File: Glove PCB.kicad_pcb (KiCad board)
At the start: 4 copper layers, 50 x 40 mm, 60 parts, among them IC2 MAX11128ATI+, IC3 MAX11128ATI+, J1 USB_B_Micro, J2 Conn_01x06_Female, J3 Conn_01x04_Female, J4 Conn_01x02_Female, J5 Conn_01x06_Female, J6 Conn_01x04_Female, J7 Conn_02x07_Odd_Even, Q1 DMG2305, Q2 BSS138, Q3 BSS138, SW1 TS-1109S-B-B, U1 MCP73831T-2ACI_OT, U2 REF3030, U3 113990582

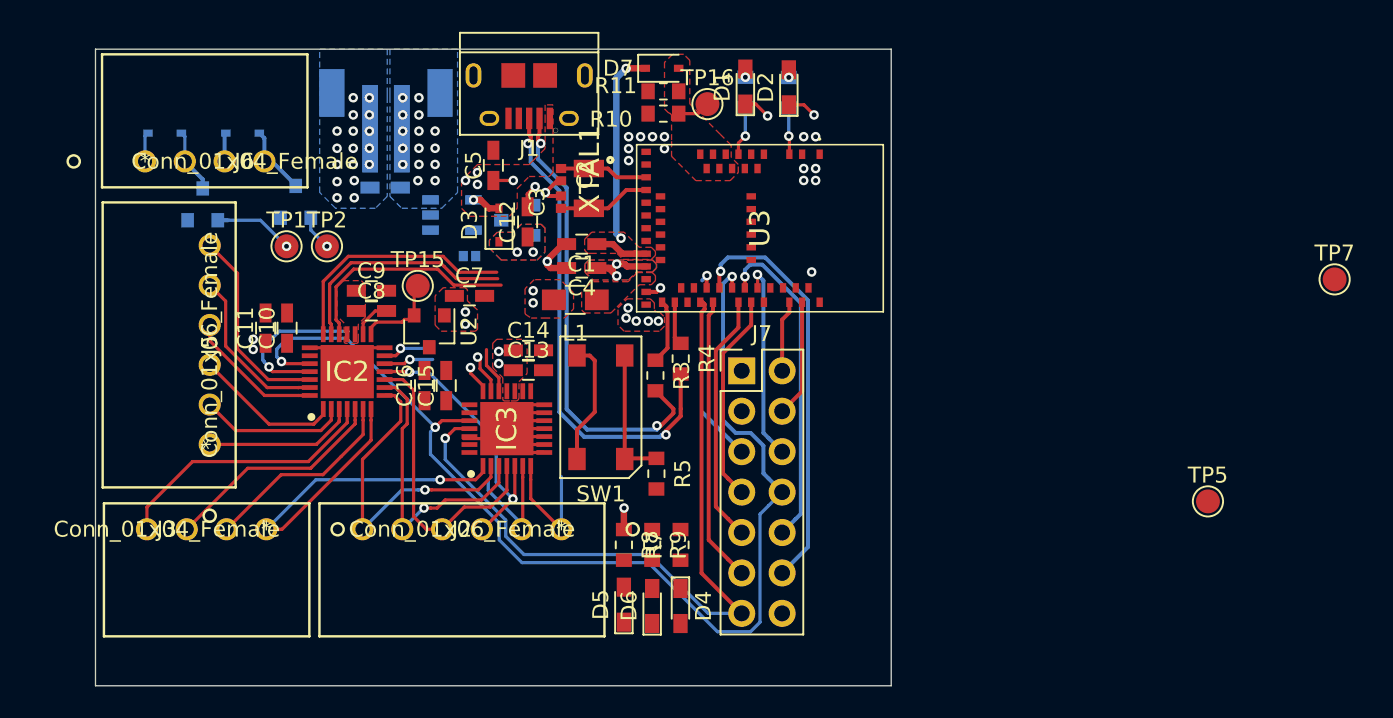
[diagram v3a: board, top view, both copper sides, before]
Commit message: Added high side R for sensors and buck-boost. Replaced 3.0V VRef with LDO. BOM rev 1. Finished layout. TODO: Silkscreen.
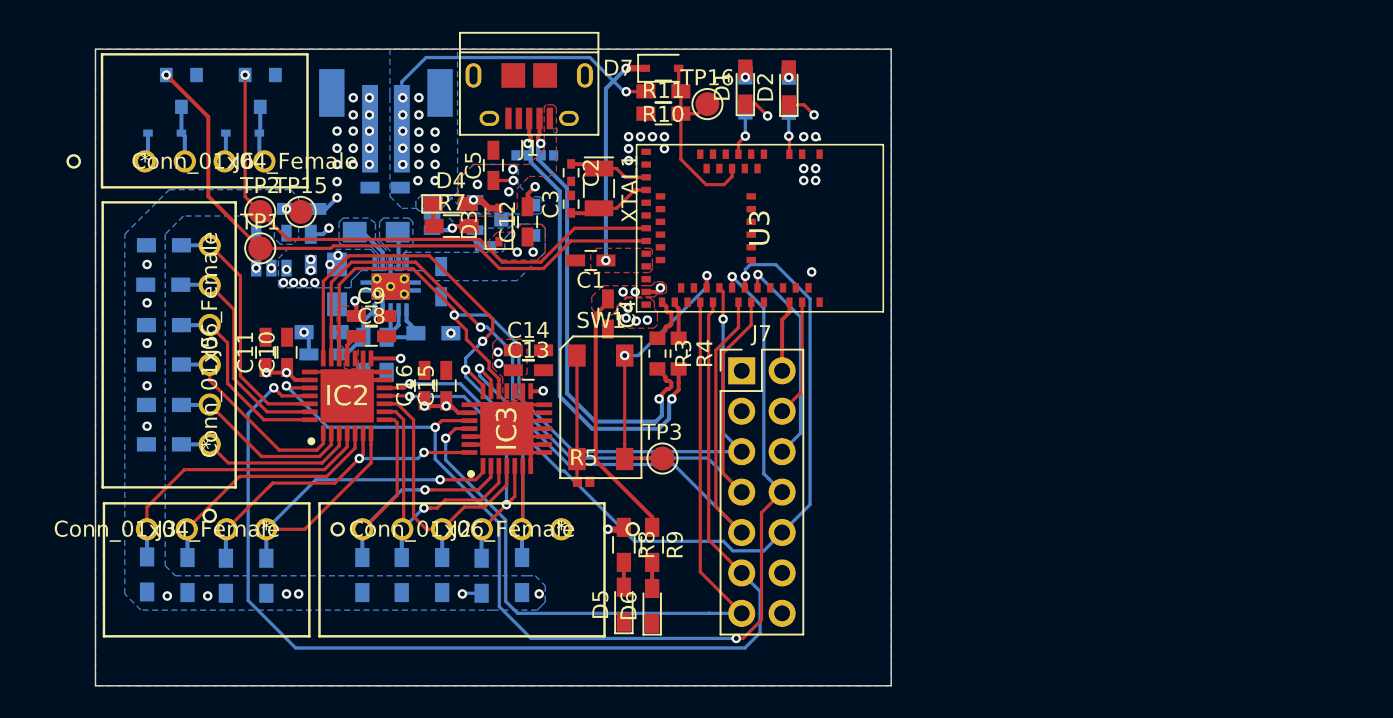
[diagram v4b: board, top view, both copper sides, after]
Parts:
- removed TP5: NFC1, TestPoint:TestPoint_Pad_D1.5mm
- removed TP7: NFC2, TestPoint:TestPoint_Pad_D1.5mm
- added C17: 10uF, Capacitors_SMD:C_0603_HandSoldering, B.Cu at (41.7, 169.6)
- added C18: 1pF, Capacitors_SMD:C_0603_HandSoldering, B.Cu at (34.4, 174.2)
- added C19: 33uF, Capacitors_SMD:C_0805_HandSoldering, B.Cu at (35.2, 169.8)
- added C20: 1uF, Capacitors_SMD:C_0603_HandSoldering, B.Cu at (33.0, 165.0)
- added D10: PGB1010402KR, Diode_SMD:D_0402_1005Metric, B.Cu at (46.8, 161.7)
- added D11: PGB1010402KR, Diode_SMD:D_0402_1005Metric, B.Cu at (48.4, 161.7)
- added R12: 100k, Resistors_SMD:R_0603_HandSoldering, B.Cu at (41.2, 172.8)
- added R13: 130k, Resistors_SMD:R_0603_HandSoldering, B.Cu at (38.3, 174.2)
- added R14: 178k, Resistors_SMD:R_0603_HandSoldering, B.Cu at (36.8, 174.2)
- added R15: 1Meg, Resistors_SMD:R_0603_HandSoldering, B.Cu at (34.2, 172.8)
- added R16: 220, Resistors_SMD:R_0603_HandSoldering, B.Cu at (24.3, 167.3)
- added R17: 220, Resistors_SMD:R_0603_HandSoldering, B.Cu at (24.3, 169.8)
- added R18: 220, Resistors_SMD:R_0603_HandSoldering, B.Cu at (24.3, 172.3)
- added R19: 220, Resistors_SMD:R_0603_HandSoldering, B.Cu at (24.3, 174.8)
- added R20: 220, Resistors_SMD:R_0603_HandSoldering, B.Cu at (24.3, 177.4)
- added R21: 220, Resistors_SMD:R_0603_HandSoldering, B.Cu at (24.3, 179.8)
- added R22: 220, Resistors_SMD:R_0603_HandSoldering, B.Cu at (23.2, 188.0)
- added R23: 220, Resistors_SMD:R_0603_HandSoldering, B.Cu at (25.8, 188.0)
- added R24: 220, Resistors_SMD:R_0603_HandSoldering, B.Cu at (28.2, 188.1)
- added R25: 220, Resistors_SMD:R_0603_HandSoldering, B.Cu at (30.7, 188.1)
- added R26: 220, Resistors_SMD:R_0603_HandSoldering, B.Cu at (36.8, 188.0)
- added R27: 220, Resistors_SMD:R_0603_HandSoldering, B.Cu at (39.2, 188.0)
- added R28: 220, Resistors_SMD:R_0603_HandSoldering, B.Cu at (41.8, 188.0)
- added R29: 220, Resistors_SMD:R_0603_HandSoldering, B.Cu at (44.3, 188.1)
- added R30: 220, Resistors_SMD:R_0603_HandSoldering, B.Cu at (46.8, 188.0)
- added TP3: RST, TestPoint:TestPoint_Pad_D1.5mm, F.Cu at (55.6, 180.7)
- added U4: TPS63000, Package_SON:VSON-10-1EP_3x3mm_P0.5mm_EP1.65x2.4mm_ThermalVias, B.Cu at (38.5, 169.9)
- C10, C13, C15, C8: value 0.1u -> 0.1uF
- C11, C14, C16, C9: value 10u -> 10uF
- C2, C3: footprint Capacitor_SMD:C_0402_1005Metric -> Capacitors_SMD:C_0402
- C7: value 0.47u -> 1uF; moved to B.Cu
- D4, D5, D6: value 19-213/Y2C-CQ2R2L/3T -> 19-213/Y2C-CQ2R2L/3T(CY)
- L1: value 10uH -> 2.2uH; moved to B.Cu
- R1, R10, R11, R2, R7, R8, R9: footprint Resistor_SMD:R_0603_1608Metric_Pad0.84x1.00mm_HandSolder -> Resistors_SMD:R_0603_HandSoldering
- R5: footprint Resistor_SMD:R_0603_1608Metric_Pad0.84x1.00mm_HandSolder -> Resistor_SMD:R_0402_1005Metric
- U2: value REF3030 -> LP5907MFX-3.0/NOPB; footprint Package_TO_SOT_SMD:SOT-23 -> Package_TO_SOT_SMD:SOT-23-5; moved to B.Cu
- XTAL1: footprint SamacSys_Parts:ECX-31B -> Crystals:Crystal_SMD_G8-2pin_3.2x1.5mm
- moved D4 29.1 mm to (42.3, 164.7), turned to 0 degrees
- moved R7 24.7 mm to (42.4, 166.1), turned to 0 degrees
- moved L1 13.2 mm to (37.6, 166.5)
- moved U2 11.1 mm to (31.0, 167.7), turned to 90 degrees
- moved C7 10.4 mm to (33.5, 167.6), turned to 90 degrees
- moved TP15 8.70 mm to (32.9, 165.2)
- moved Q3 7.32 mm to (30.4, 157.6), turned to 270 degrees
- moved Q2 7.25 mm to (25.4, 157.6), turned to 270 degrees
- moved TP2 4.71 mm to (30.4, 165.2)
- moved R5 4.60 mm to (50.7, 182.2), turned to 0 degrees
- moved C4 3.32 mm to (52.2, 171.6), turned to 270 degrees
- moved TP1 1.66 mm to (30.4, 167.5)
- moved C8 1.59 mm to (37.3, 173.0)
- moved C9 1.59 mm to (37.3, 171.8)
- moved C10 1.52 mm to (32.0, 174.1)
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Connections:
- C4 pad 1: VDD -> VBUS
- D8 pad 1: +3V3 -> VDD
- D9 pad 1: +3V3 -> VDD
- IC2 pad 13: /Sensors/A0 -> GND
- IC3 pad 7: /Sensors/A0 -> GND
- J2 pad 1: /Sensors/A0 -> GND
- J6 pad 1: +3V3 -> VDD
- J6 pad 3: +3V3 -> VDD
- J7 pad 12: /SCK -> GND
- J7 pad 5: /RST -> /SCK
- L1 pad 1: Net-(L1-Pad1) -> /Power/L1
- L1 pad 2: +3V3 -> /Power/L2
- U2 pad 2: /AREF -> GND
- U2 pad 3: GND -> +3V3
- U3 pad 24: Net-(U3-Pad24) -> /H1
- U3 pad 26: Net-(U3-Pad26) -> /H0
- U3 pad 30: VDD -> +3V3
- U3 pad 31: Net-(L1-Pad1) -> Net-(U3-Pad31)
- U3 pad 52: /NFC1 -> Net-(U3-Pad52)
- U3 pad 54: /NFC2 -> Net-(U3-Pad54)
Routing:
- net /~EOC0: track 27.9 -> 72.5 mm
- net /H0: track 5.65 -> 39.0 mm
- net /H1: track 2.21 -> 35.4 mm
- net /MOSI: track 37.8 -> 70.5 mm, vias 2 -> 3
- net /AREF: track 5.41 -> 36.6 mm, vias 0 -> 14
- net /~CS0: track 27.9 -> 52.1 mm, vias 0 -> 1
- net /~CS1: track 18.2 -> 38.5 mm
- net +BATT: track 0.00 -> 19.8 mm, vias 13 -> 14
- net GND: track 41.0 -> 58.2 mm, vias 25 -> 30
- net VBUS: track 4.08 -> 20.2 mm, vias 6 -> 8
- net /Sensors/A0: track 11.4 -> 0.00 mm, vias 1 -> 0
- net /SCK: track 43.3 -> 54.2 mm, vias 1 -> 2
- net /Sensors/A1: track 11.1 -> 21.9 mm
- net /VBATT_OUT: track 2.05 -> 12.4 mm
- net /Sensors/A7: track 12.6 -> 21.3 mm, vias 0 -> 2
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- added copper zone on B.Cu, net +3V3
- added copper zone on B.Cu, net /AREF
- added copper zone on In1.Cu, net /AREF
- added copper zone on B.Cu, net /Power/L1
- added copper zone on B.Cu, net /Power/L2
- added copper zone on B.Cu, net VBUS
- removed copper zone on B.Cu, net (none)
- removed copper zone on F.Cu, net (none)
- removed copper zone on F.Cu, net /VBATT_OUT
- removed copper zone on F.Cu, net Net-(L1-Pad1)

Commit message: Filled copper zone priorities were frickle-frackled, they are fixed now. Still gotta do silk :(
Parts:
- moved R6 1.08 mm to (43.4, 167.4), turned to 180 degrees
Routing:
- net GND: track 58.2 -> 61.9 mm, vias 30 -> 80
- net (no net): vias 10 -> 3
- added copper zone on In1.Cu, net GND
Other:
- board size 50 x 40 mm -> 50 x 38 mm

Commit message: My nap was too long but finished silk.
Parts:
- HP FB: renamed from J6
- moved C4 1.34 mm to (51.1, 170.9), turned to 180 degrees
- moved R6 1.02 mm to (44.5, 167.4), turned to 0 degrees
- renumbered TP3 to RST
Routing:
- net GND: track 61.9 -> 64.8 mm, vias 80 -> 79
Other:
- board text added: "3V3 GND SCK CS0 CS1 EOC0 EOC1"
- board text added: "SWDIO SWDCLK SWO MISO MOSI GND GND"

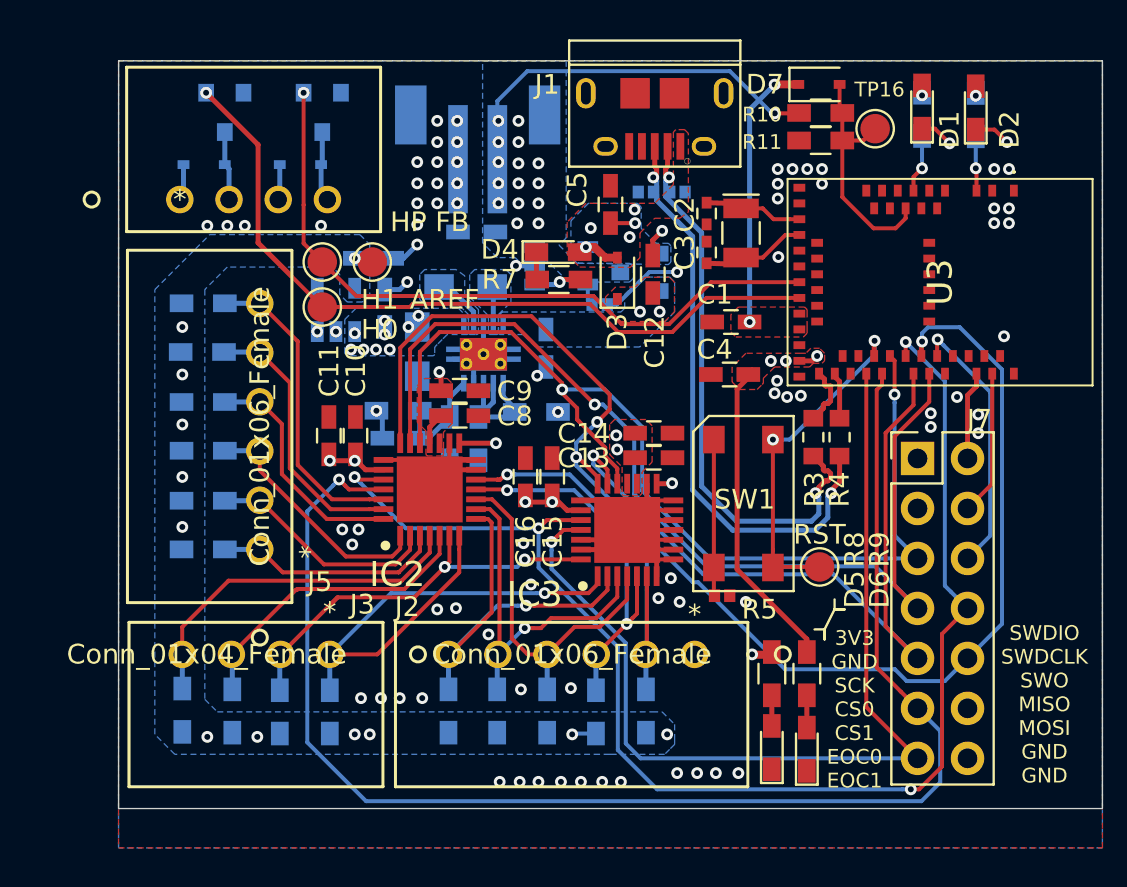
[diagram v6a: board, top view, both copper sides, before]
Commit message: Add BOM Script and generated picknplace, BOM, & Gerbers. Sent to fabgit add -A!
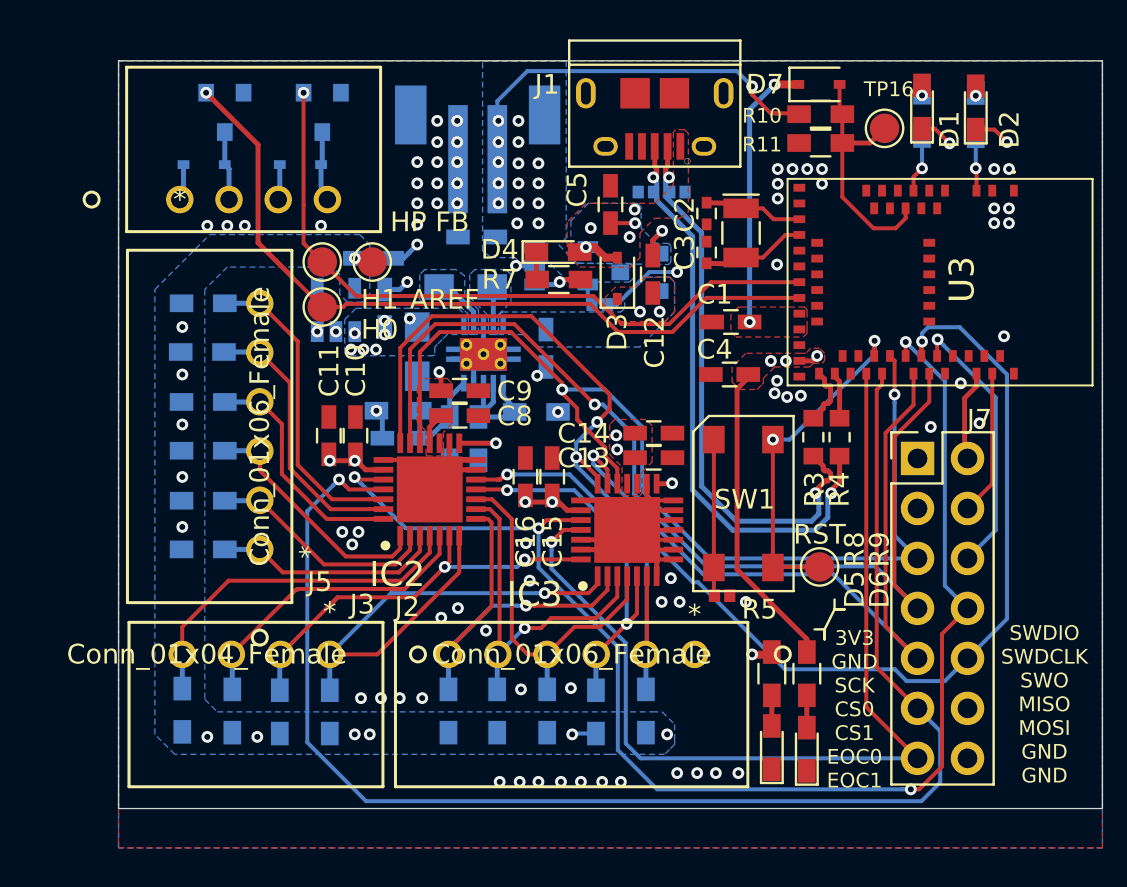
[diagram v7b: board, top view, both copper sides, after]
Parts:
- moved TP16 0.48 mm to (58.9, 158.4)
- moved C6 0.25 mm to (38.2, 164.0)
- moved R11 0.13 mm to (55.7, 159.2)
- moved R10 0.06 mm to (55.7, 157.7)
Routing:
- net GND: vias 79 -> 77
- net +3V3: vias 21 -> 19
